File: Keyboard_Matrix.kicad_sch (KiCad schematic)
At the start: 210 parts, among them SW2 RotaryEncoder_Switch_MP

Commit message: Added the OLED SPI Display and remade the entire PCB
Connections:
- no-connect marks 0 -> 1
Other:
- moved on the sheet: CH1, CH10, CH100, CH101, CH102, CH103, CH104, CH11, CH12, CH13, CH14, CH15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

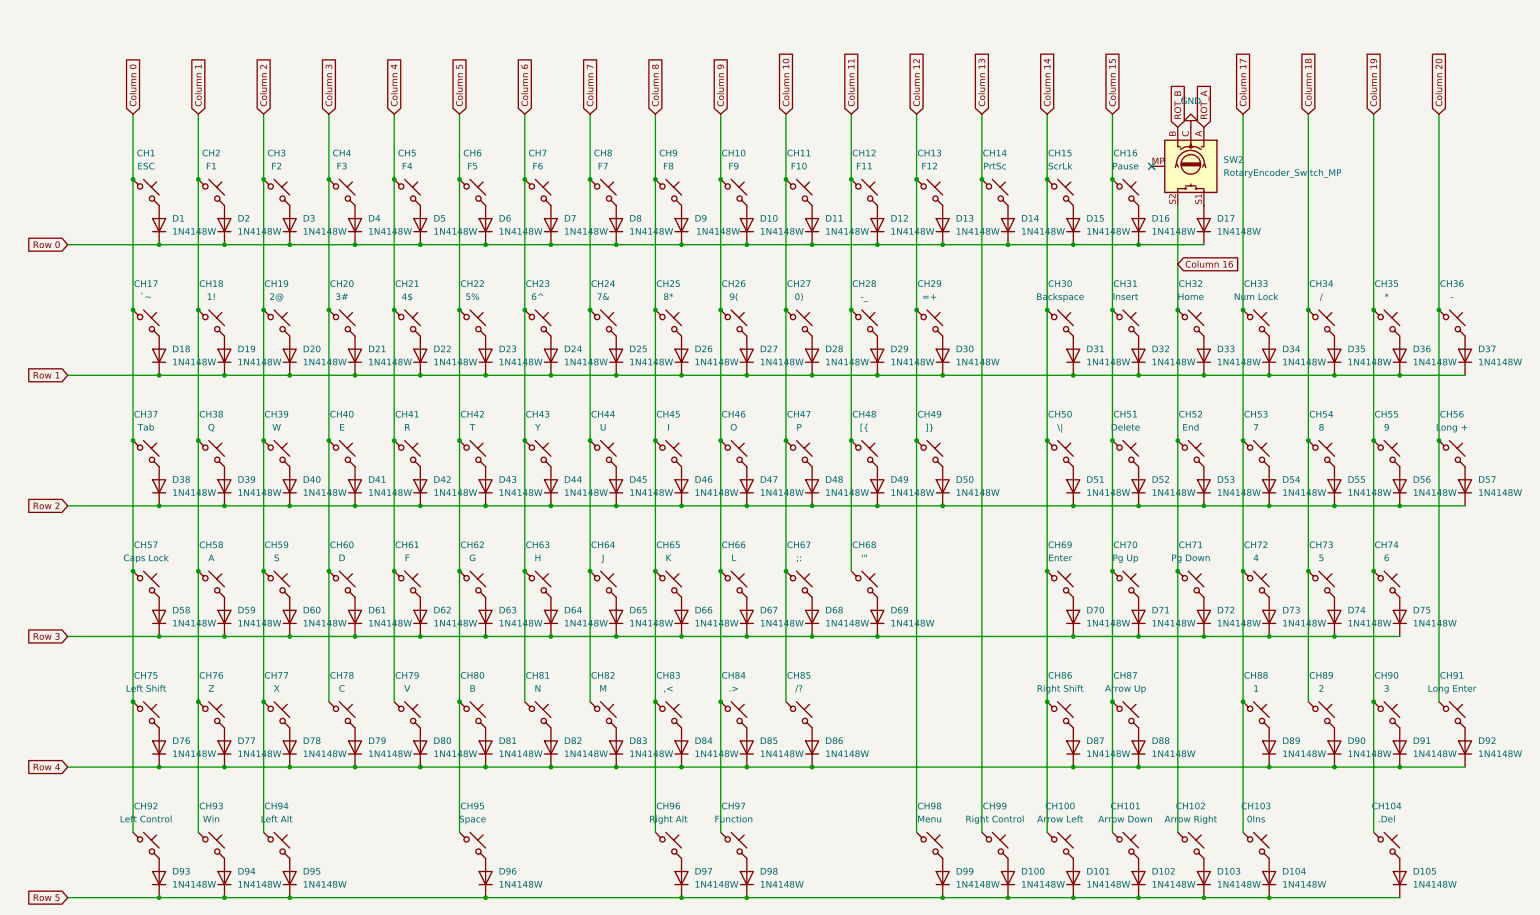
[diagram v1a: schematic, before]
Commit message: Replaced Rotary Encoder.
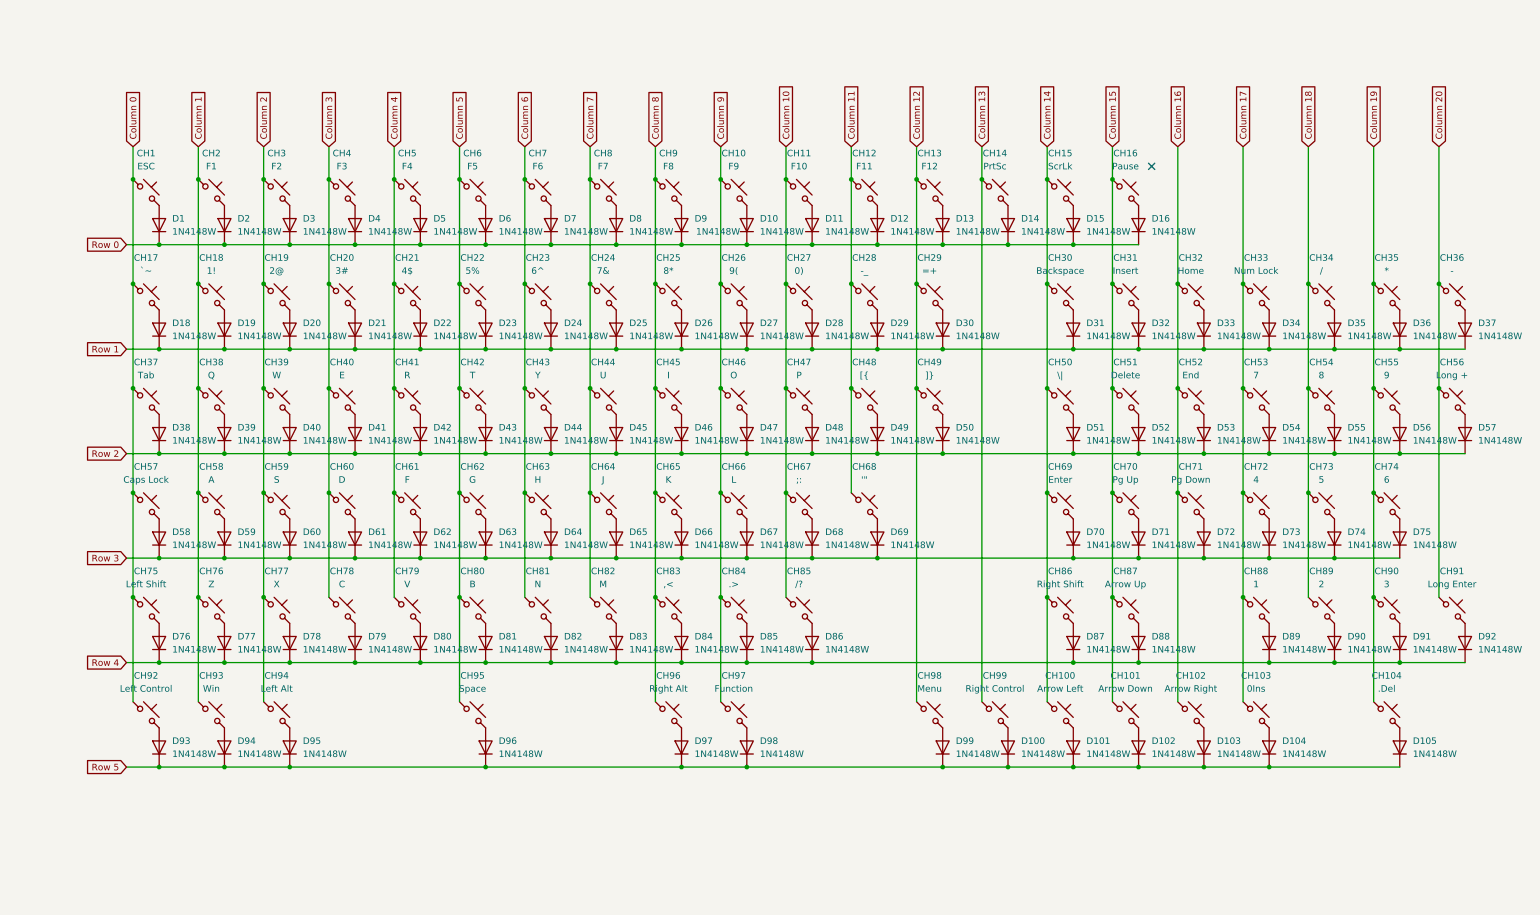
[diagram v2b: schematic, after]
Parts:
- removed D17: 1N4148W, Diode_SMD:D_SOD-123, symbol Diode:1N4148W
- removed SW2: RotaryEncoder_Switch_MP, Rotary_Encoder:RotaryEncoder_Alps_EC11E-Switch_Vertical_H20mm_CircularMountingHoles, symbol Device:RotaryEncoder_Switch_MP
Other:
- moved on the sheet: CH100, CH101, CH102, CH103, CH104, CH17, CH18, CH19, CH20, CH21, CH22, CH23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
